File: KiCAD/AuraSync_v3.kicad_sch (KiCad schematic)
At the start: 9 parts, among them J1 Battery, Q1 2N2222, U1 ESP32S3, U2 MT3608, U3 BME680, U4 HC-SR501PIR, U5 SPH0645_Mic

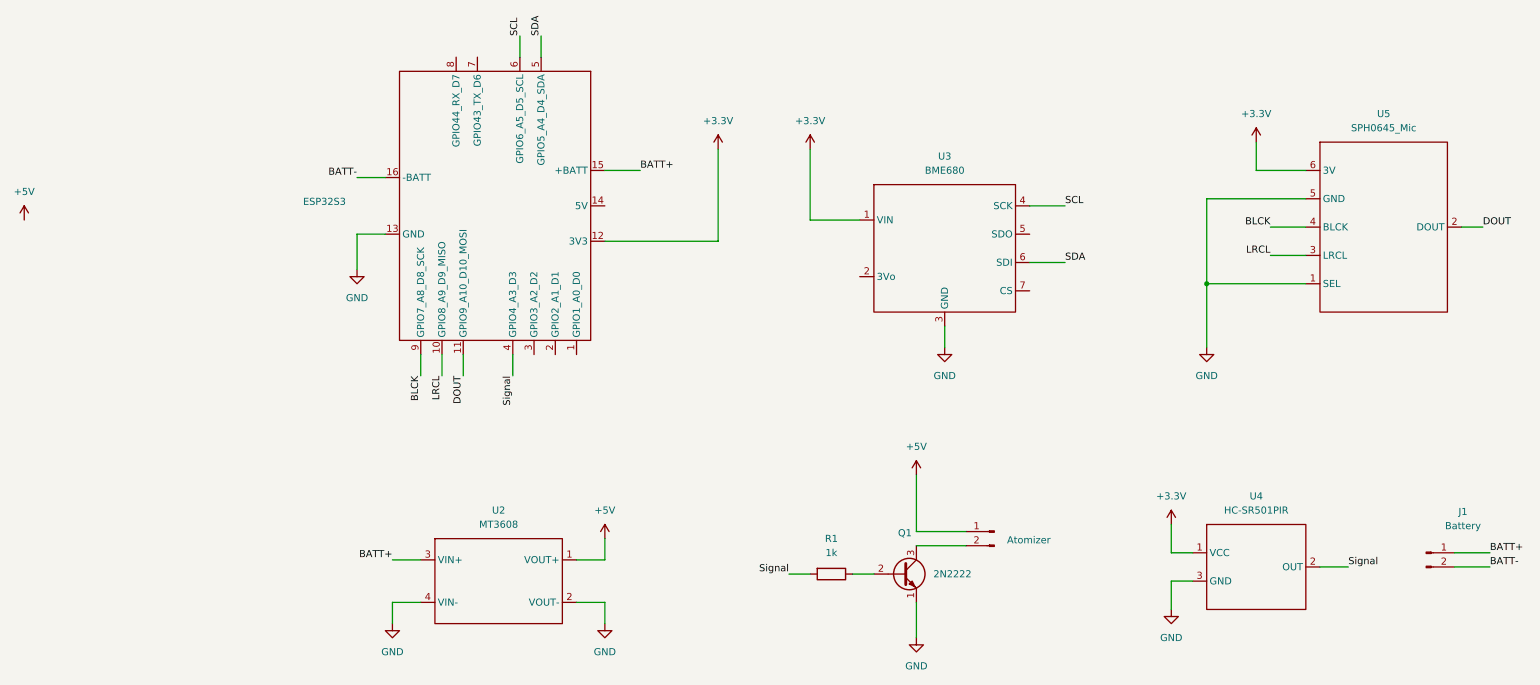
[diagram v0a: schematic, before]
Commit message: Add week-06 devlog, fix week-03/05 status, update homepage credits
- week-06.md / week-06.zh.md: new entry covering ML on-device inference
  (C weight array export, Round 2 Val F1 0.902), Firebase reverse control
  validation, Enclosure v2 cylindrical snap-fit, PCB v1 LPKF fabrication
- week-05.md: status → Completed; tick shower, enclosure, PCB checkboxes
- week-03.md / week-03.zh.md: status → Completed
- strings.js: add Week 6 credits for both team members; update roles/bios
- DevlogMarkdownBody.jsx: add enclosure-concept-embed and enclosure-printed-embed
- Add PCB and enclosure images to public/images/devlog/

Co-Authored-By: Claude Sonnet 4.6 <noreply@anthropic.com>
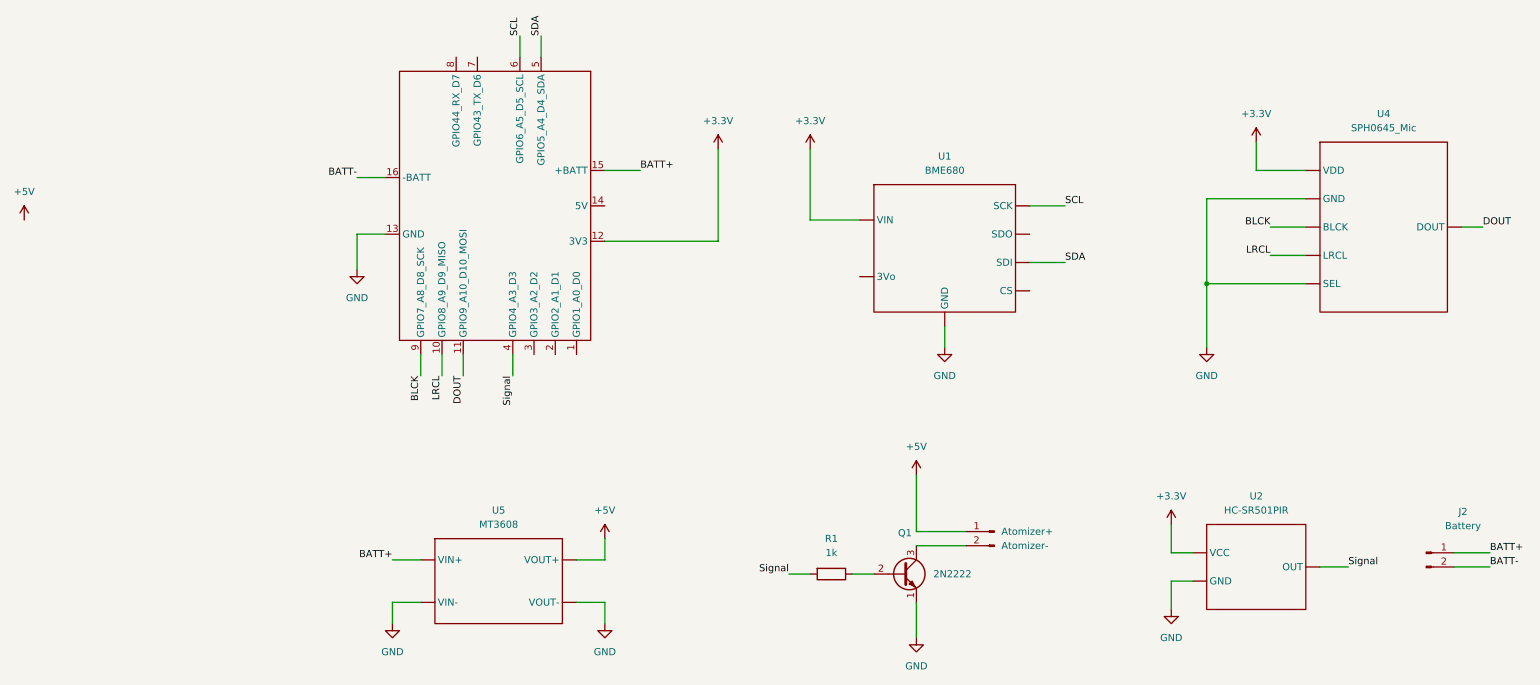
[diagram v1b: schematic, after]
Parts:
- Atomizer-: renamed from Atomizer-1; value Atomizer -> Atomizer+; footprint Connector_PinSocket_2.54mm:PinSocket_1x02_P2.54mm_Vertical -> (none)
- J2: renamed from J1; footprint Connector_PinSocket_2.54mm:PinSocket_1x02_P2.54mm_Vertical -> (none)
- Q1: footprint Connector_PinSocket_2.54mm:PinSocket_1x03_P2.54mm_Vertical -> Package_TO_SOT_THT:TO-39-3
- R1: footprint Resistor_SMD:R_0603_1608Metric_Pad0.98x0.95mm_HandSolder -> (none)
- U1: renamed from U3; footprint Connector_PinSocket_2.54mm:PinSocket_1x07_P2.54mm_Vertical -> (none)
- U2: renamed from U1; value ESP32S3 -> ~; footprint ESP32_Xiao_Seeed_GIX:XIAO_ESP32 -> (none)
- U2: renamed from U4; footprint Connector_PinSocket_2.54mm:PinSocket_1x03_P2.54mm_Vertical -> (none)
- U4: renamed from U5; footprint Connector_PinSocket_2.54mm:PinSocket_1x06_P2.54mm_Vertical -> (none)
- U5: renamed from U2; footprint AuraSync:MT3608 -> (none)
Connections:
- net +3.3V: now also U1. (CS), U2. (OUT), U4. (DOUT); no longer U1.1 (VIN), U2.1 (VCC), U4.6 (3V)
- net +5V: now also U5. (VOUT-); no longer U5.1 (VOUT+)
- net BATT+: now also U5. (VOUT-); no longer U5.3 (VIN+)
- net BLCK: now also U4. (DOUT); no longer U4.4 (BLCK)
- net DOUT: now also U4. (DOUT); no longer U4.2 (DOUT)
- net GND: now also U1. (CS), U2. (OUT), U4. (DOUT), U5. (VOUT-); no longer U1.3 (GND), U2.3 (GND), U4.1 (SEL), U4.5 (GND), U5.2 (VOUT-), U5.4 (VIN-)
- net LRCL: now also U4. (DOUT); no longer U4.3 (LRCL)
- net SCL: now also U1. (CS); no longer U1.4 (SCK)
- net SDA: now also U1. (CS); no longer U1.6 (SDI)
- net Signal: now also U2. (OUT); no longer U2.2 (OUT)
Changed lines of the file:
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@@
 		(dnp no)
 		(fields_autoplaced yes)
-		(property "Reference" "#PWR09"
+		(property "Reference" "#PWR010"
 			(at 158.75 148.59 0)
 			(effects
@@
 			(project "AuraSync_v2"
 				(path "/f6a34317-bbb6-43a9-bbfc-b31c8103131a"
-					(reference "#PWR09")
+					(reference "#PWR010")
 					(unit 1)
 				)
@@
 		(dnp no)
 		(fields_autoplaced yes)
-		(property "Reference" "#PWR01"
+		(property "Reference" "#PWR03"
 			(at -1.27 71.12 0)
 			(effects
@@
 			(project ""
 				(path "/f6a34317-bbb6-43a9-bbfc-b31c8103131a"
-					(reference "#PWR01")
+					(reference "#PWR03")
 					(unit 1)
 				)
@@
 		(on_board yes)
 		(dnp no)
-		(property "Reference" "U1"
+		(fields_autoplaced yes)
+		(property "Reference" "U2"
 			(at 83.566 29.21 0)
 			(effects
@@
 			)
 		)
-		(property "Value" "ESP32S3"
-			(at 52.578 64.008 90)
-			(effects
-				(font
-					(size 1.27 1.27)
-				)
-			)
-		)
-		(property "Footprint" "ESP32_Xiao_Seeed_GIX:XIAO_ESP32"
+		(property "Value" "~"
+			(at 66.04 57.0798 90)
+			(effects
+				(font
+					(size 1.27 1.27)
+				)
+			)
+		)
+		(property "Footprint" ""
 			(at 83.82 64.77 0)
 			(effects
@@
 			(project ""
 				(path "/f6a34317-bbb6-43a9-bbfc-b31c8103131a"
-					(reference "U1")
+					(reference "U2")
 					(unit 1)
 				)
@@
 		(dnp no)
 		(fields_autoplaced yes)
-		(property "Reference" "#PWR012"
+		(property "Reference" "#PWR014"
 			(at 204.47 143.51 0)
 			(effects
@@
 			(project "AuraSync_v2"
 				(path "/f6a34317-bbb6-43a9-bbfc-b31c8103131a"
-					(reference "#PWR012")
+					(reference "#PWR014")
 					(unit 1)
 				)
@@
 		(on_board yes)
 		(dnp no)
-		(property "Reference" "J1"
+		(property "Reference" "J2"
 			(at 256.794 119.634 0)
 			(effects
@@
 			)
 		)
-		(property "Footprint" "Connector_PinSocket_2.54mm:PinSocket_1x02_P2.54mm_Vertical"
+		(property "Footprint" ""
 			(at 250.19 127 0)
 			(effects
@@
 			(project "AuraSync_v1"
 				(path "/f6a34317-bbb6-43a9-bbfc-b31c8103131a"
-					(reference "J1")
+					(reference "J2")
 					(unit 1)
 				)
@@
 		(dnp no)
 		(fields_autoplaced yes)
-		(property "Reference" "U4"
+		(property "Reference" "U2"
 			(at 219.71 116.84 0)
 			(effects
@@
 			)
 		)
-		(property "Footprint" "Connector_PinSocket_2.54mm:PinSocket_1x03_P2.54mm_Vertical"
-			(at 220.218 135.382 0)
+		(property "Footprint" ""
+			(at 219.71 129.54 0)
 			(effects
 				(font
@@
 			)
 		)
-		(pin "2"
-		)
-		(pin "1"
-		)
-		(pin "3"
+		(pin ""
+		)
+		(pin ""
+		)
+		(pin ""
 		)
 		(instances
 			(project ""
 				(path "/f6a34317-bbb6-43a9-bbfc-b31c8103131a"
-					(reference "U4")
+					(reference "U2")
 					(unit 1)
 				)
@@
 		(dnp no)
 		(fields_autoplaced yes)
-		(property "Reference" "#PWR010"
+		(property "Reference" "#PWR06"
 			(at 163.83 96.52 0)
 			(effects
@@
 			(project "AuraSync_v1"
 				(path "/f6a34317-bbb6-43a9-bbfc-b31c8103131a"
-					(reference "#PWR010")
+					(reference "#PWR06")
 					(unit 1)
 				)
@@
 		(dnp no)
 		(fields_autoplaced yes)
-		(property "Reference" "#PWR08"
+		(property "Reference" "#PWR09"
 			(at 158.75 116.84 0)
 			(effects
@@
 			(project "AuraSync_v2"
 				(path "/f6a34317-bbb6-43a9-bbfc-b31c8103131a"
-					(reference "#PWR08")
+					(reference "#PWR09")
 					(unit 1)
 				)
@@
 		(dnp no)
 		(fields_autoplaced yes)
-		(property "Reference" "#PWR013"
+		(property "Reference" "#PWR012"
 			(at 210.82 96.52 0)
 			(effects
@@
 			(project "AuraSync_v2"
 				(path "/f6a34317-bbb6-43a9-bbfc-b31c8103131a"
-					(reference "#PWR013")
+					(reference "#PWR012")
 					(unit 1)
 				)
@@
 		(dnp no)
 		(fields_autoplaced yes)
-		(property "Reference" "U2"
+		(property "Reference" "U5"
 			(at 83.82 119.38 0)
 			(effects
@@
 			)
 		)
-		(property "Footprint" "AuraSync:MT3608"
+		(property "Footprint" ""
 			(at 83.82 132.08 0)
 			(effects
@@
 			)
 		)
-		(pin "2"
-		)
-		(pin "3"
-		)
-		(pin "1"
-		)
-		(pin "4"
+		(pin ""
+		)
+		(pin ""
+		)
+		(pin ""
+		)
+		(pin ""
 		)
 		(instances
 			(project ""
 				(path "/f6a34317-bbb6-43a9-bbfc-b31c8103131a"
-					(reference "U2")
+					(reference "U5")
 					(unit 1)
 				)
@@
 		(on_board yes)
 		(dnp no)
-		(property "Reference" "#PWR011"
+		(property "Reference" "#PWR013"
 			(at 204.47 125.73 0)
 			(effects
@@
 			(project "AuraSync_v2"
 				(path "/f6a34317-bbb6-43a9-bbfc-b31c8103131a"
-					(reference "#PWR011")
+					(reference "#PWR013")
 					(unit 1)
 				)
@@
 		(dnp no)
 		(fields_autoplaced yes)
-		(property "Reference" "U5"
+		(property "Reference" "U4"
 			(at 242.57 48.26 0)
 			(effects
@@
 			)
 		)
-		(property "Footprint" "Connector_PinSocket_2.54mm:PinSocket_1x06_P2.54mm_Vertical"
+		(property "Footprint" ""
 			(at 242.57 64.77 0)
 			(effects
@@
 			)
 		)
-		(pin "6"
-		)
-		(pin "5"
-		)
-		(pin "2"
-		)
-		(pin "4"
-		)
-		(pin "3"
-		)
-		(pin "1"
+		(pin ""
+		)
+		(pin ""
+		)
+		(pin ""
+		)
+		(pin ""
+		)
+		(pin ""
+		)
+		(pin ""
 		)
 		(instances
 			(project ""
 				(path "/f6a34317-bbb6-43a9-bbfc-b31c8103131a"
-					(reference "U5")
+					(reference "U4")
 					(unit 1)
 				)
@@
 		(dnp no)
 		(fields_autoplaced yes)
-		(property "Reference" "U3"
+		(property "Reference" "U1"
 			(at 163.83 55.88 0)
 			(effects
@@
 			)
 		)
-		(property "Footprint" "Connector_PinSocket_2.54mm:PinSocket_1x07_P2.54mm_Vertical"
+		(property "Footprint" ""
 			(at 163.83 72.39 0)
 			(effects
@@
 			)
 		)
-		(pin "2"
-		)
-		(pin "7"
-		)
-		(pin "3"
-		)
-		(pin "5"
-		)
-		(pin "6"
-		)
-		(pin "4"
-		)
-		(pin "1"
+		(pin ""
+		)
+		(pin ""
+		)
+		(pin ""
+		)
+		(pin ""
+		)
+		(pin ""
+		)
+		(pin ""
+		)
+		(pin ""
 		)
 		(instances
 			(project ""
 				(path "/f6a34317-bbb6-43a9-bbfc-b31c8103131a"
-					(reference "U3")
+					(reference "U1")
 					(unit 1)
 				)
@@
 		(dnp no)
 		(fields_autoplaced yes)
-		(property "Reference" "#PWR02"
+		(property "Reference" "#PWR05"
 			(at 58.42 82.55 0)
 			(effects
@@
 			(project ""
 				(path "/f6a34317-bbb6-43a9-bbfc-b31c8103131a"
-					(reference "#PWR02")
+					(reference "#PWR05")
 					(unit 1)
 				)
@@
 		(on_board yes)
 		(dnp no)
-		(property "Reference" "Atomizer-1"
+		(property "Reference" "Atomizer-"
 			(at 173.99 125.73 0)
 			(effects
@@
 				)
 				(justify right)
-				(hide yes)
-			)
-		)
-		(property "Value" "Atomizer"
-			(at 175.006 124.714 0)
+			)
+		)
+		(property "Value" "Atomizer+"
+			(at 173.99 123.1901 0)
 			(effects
 				(font
@@
 			)
 		)
-		(property "Footprint" "Connector_PinSocket_2.54mm:PinSocket_1x02_P2.54mm_Vertical"
+		(property "Footprint" ""
 			(at 172.72 123.19 0)
 			(effects
@@
 			(project "AuraSync_v2"
 				(path "/f6a34317-bbb6-43a9-bbfc-b31c8103131a"
-					(reference "Atomizer-1")
+					(reference "Atomizer-")
 					(unit 1)
 				)
@@
 			)
 		)
-		(property "Footprint" "Connector_PinSocket_2.54mm:PinSocket_1x03_P2.54mm_Vertical"
+		(property "Footprint" "Package_TO_SOT_THT:TO-39-3"
 			(at 161.29 132.715 0)
 			(effects
@@
 			)
 		)
-		(property "Footprint" "Resistor_SMD:R_0603_1608Metric_Pad0.98x0.95mm_HandSolder"
+		(property "Footprint" ""
 			(at 143.51 129.032 90)
 			(effects
@@
 		(on_board yes)
 		(dnp no)
-		(property "Reference" "#PWR06"
+		(property "Reference" "#PWR01"
 			(at 123.19 58.42 0)
 			(effects
@@
 			(project ""
 				(path "/f6a34317-bbb6-43a9-bbfc-b31c8103131a"
-					(reference "#PWR06")
+					(reference "#PWR01")
 					(unit 1)
 				)
@@
 		(on_board yes)
 		(dnp no)
-		(property "Reference" "#PWR014"
+		(property "Reference" "#PWR011"
 			(at 219.71 57.15 0)
 			(effects
@@
 			(project "AuraSync_v2"
 				(path "/f6a34317-bbb6-43a9-bbfc-b31c8103131a"
-					(reference "#PWR014")
+					(reference "#PWR011")
 					(unit 1)
 				)
@@
 		(dnp no)
 		(fields_autoplaced yes)
-		(property "Reference" "#PWR03"
+		(property "Reference" "#PWR07"
 			(at 64.77 146.05 0)
 			(effects
@@
 			(project "AuraSync_v1"
 				(path "/f6a34317-bbb6-43a9-bbfc-b31c8103131a"
-					(reference "#PWR03")
+					(reference "#PWR07")
 					(unit 1)
 				)
@@
 		(dnp no)
 		(fields_autoplaced yes)
-		(property "Reference" "#PWR05"
+		(property "Reference" "#PWR08"
 			(at 102.87 146.05 0)
 			(effects
@@
 			(project "AuraSync_v1"
 				(path "/f6a34317-bbb6-43a9-bbfc-b31c8103131a"
-					(reference "#PWR05")
+					(reference "#PWR08")
 					(unit 1)
 				)
@@
 		(dnp no)
 		(fields_autoplaced yes)
-		(property "Reference" "#PWR07"
+		(property "Reference" "#PWR02"
 			(at 139.7 58.42 0)
 			(effects
@@
 			(project "AuraSync_v1"
 				(path "/f6a34317-bbb6-43a9-bbfc-b31c8103131a"
-					(reference "#PWR07")
-					(unit 1)
-				)
+					(reference "#PWR02")
+					(unit 1)
+				)
